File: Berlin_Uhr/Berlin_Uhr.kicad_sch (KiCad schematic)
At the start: 53 parts, among them J1 USB_C_Receptacle_USB2.0, J2 ISP, Q1 KPS-3227, SW1 SW_Push, SW2 SW_Push, U1 DS3231M, U2 ATtiny167-SU, U3 TLC5947DAP, Y1 16MHz

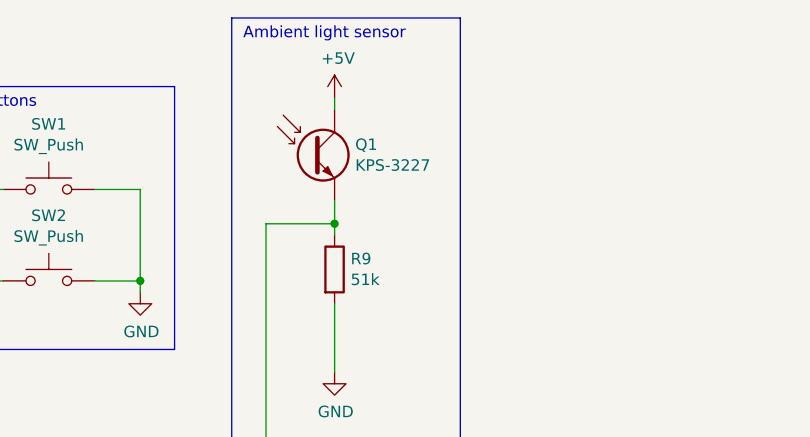
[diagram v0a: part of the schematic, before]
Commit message: Switch KPS-3227 to native KiCad part.
KiCad 6.0.2 fixed the KPS-3227 Footprint, now using the build in one.
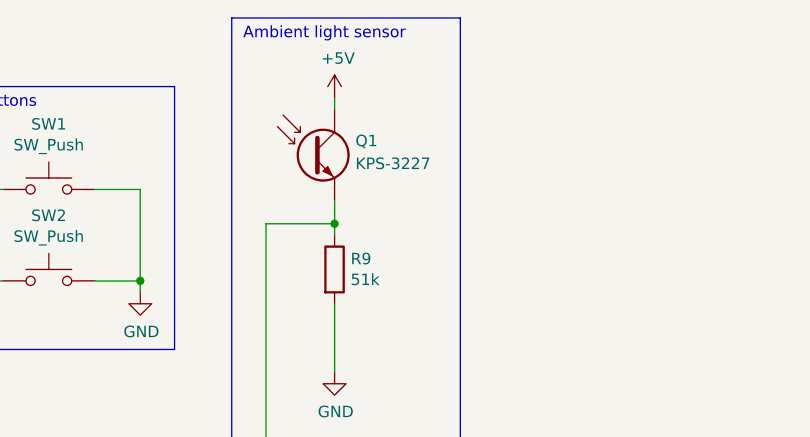
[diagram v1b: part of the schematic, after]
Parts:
- removed Q1: KPS-3227, Berlin_Uhr:Kingbright_KPS-3227, symbol Berlin_Uhr:KPS-3227
- added Q1: KPS-3227, OptoDevice:Kingbright_KPS-3227, symbol Sensor_Optical:KPS-3227
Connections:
- net +5V: now also Q1.1, Q1.3
- net at R9.1, U2.9 (PA6): now also Q1.2, Q1.4
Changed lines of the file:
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@@
     (pin "1")
-  )
-  (symbol (lib_id "Berlin_Uhr:KPS-3227") (at 185.42 29.21 0) (unit 1)
-    (in_bom yes) (on_board yes)
-    (property "Reference" "Q1" (id 0) (at 187.706 28.0416 0)
-      (effects (font (size 1.27 1.27)) (justify left))
-    )
-    (property "Value" "KPS-3227" (id 1) (at 187.706 30.353 0)
-      (effects (font (size 1.27 1.27)) (justify left))
-    )
-    (property "Footprint" "Berlin_Uhr:Kingbright_KPS-3227" (id 2) (at 185.42 25.4 0)
-      (effects (font (size 1.27 1.27)) hide)
-    )
-    (property "Datasheet" "https://www.kingbright.com/attachments/file/psearch/000/00/00/KPS-3227SP1C(Ver.16).pdf" (id 3) (at 185.42 25.4 0)
-      (effects (font (size 1.27 1.27)) hide)
-    )
-    (pin "1")
-    (pin "2")
-    (pin "3")
-    (pin "4")
   )
   (symbol (lib_id "Device:R") (at 185.42 41.91 0) (unit 1)
@@
     (pin "1")
   )
+  (symbol (lib_id "Sensor_Optical:KPS-3227") (at 185.42 29.21 0) (unit 1)
+    (in_bom yes) (on_board yes) (fields_autoplaced)
+    (property "Reference" "Q1" (id 0) (at 187.7314 27.626 0)
+      (effects (font (size 1.27 1.27)) (justify left))
+    )
+    (property "Value" "KPS-3227" (id 1) (at 187.7314 30.1629 0)
+      (effects (font (size 1.27 1.27)) (justify left))
+    )
+    (property "Footprint" "OptoDevice:Kingbright_KPS-3227" (id 2) (at 185.42 25.4 0)
+      (effects (font (size 1.27 1.27)) hide)
+    )
+    (property "Datasheet" "https://www.kingbright.com/attachments/file/psearch/000/00/00/KPS-3227SP1C(Ver.16).pdf" (id 3) (at 185.42 25.4 0)
+      (effects (font (size 1.27 1.27)) hide)
+    )
+    (pin "1")
+    (pin "2")
+    (pin "3")
+    (pin "4")
+  )
   (sheet_instances
     (path "/" (page "1"))
@@
       (reference "J2") (unit 1) (value "ISP") (footprint "Connector_PinHeader_1.27mm:PinHeader_1x06_P1.27mm_Vertical")
     )
-    (path "/00000000-0000-0000-0000-00006176ee75"
-      (reference "Q1") (unit 1) (value "KPS-3227") (footprint "Berlin_Uhr:Kingbright_KPS-3227")
+    (path "/aff00d57-63ea-46b6-99f8-32eff51e9707"
+      (reference "Q1") (unit 1) (value "KPS-3227") (footprint "OptoDevice:Kingbright_KPS-3227")
     )
     (path "/00000000-0000-0000-0000-0000616fbe63"
